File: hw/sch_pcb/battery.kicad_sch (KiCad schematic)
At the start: 88 parts

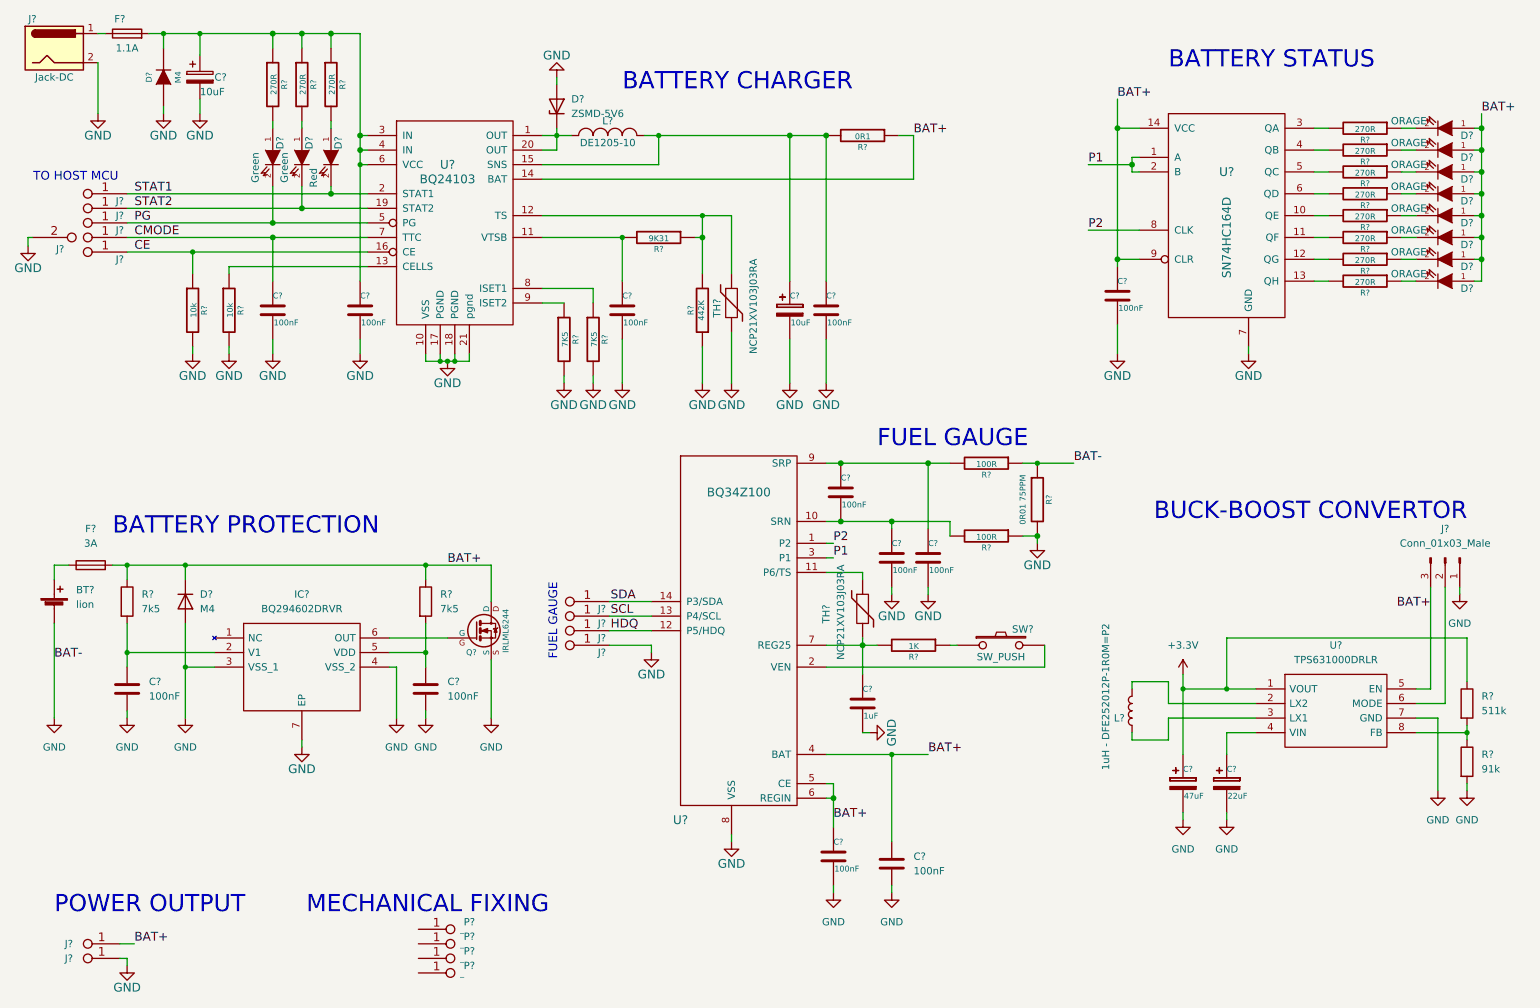
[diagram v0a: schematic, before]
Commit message: schematics update
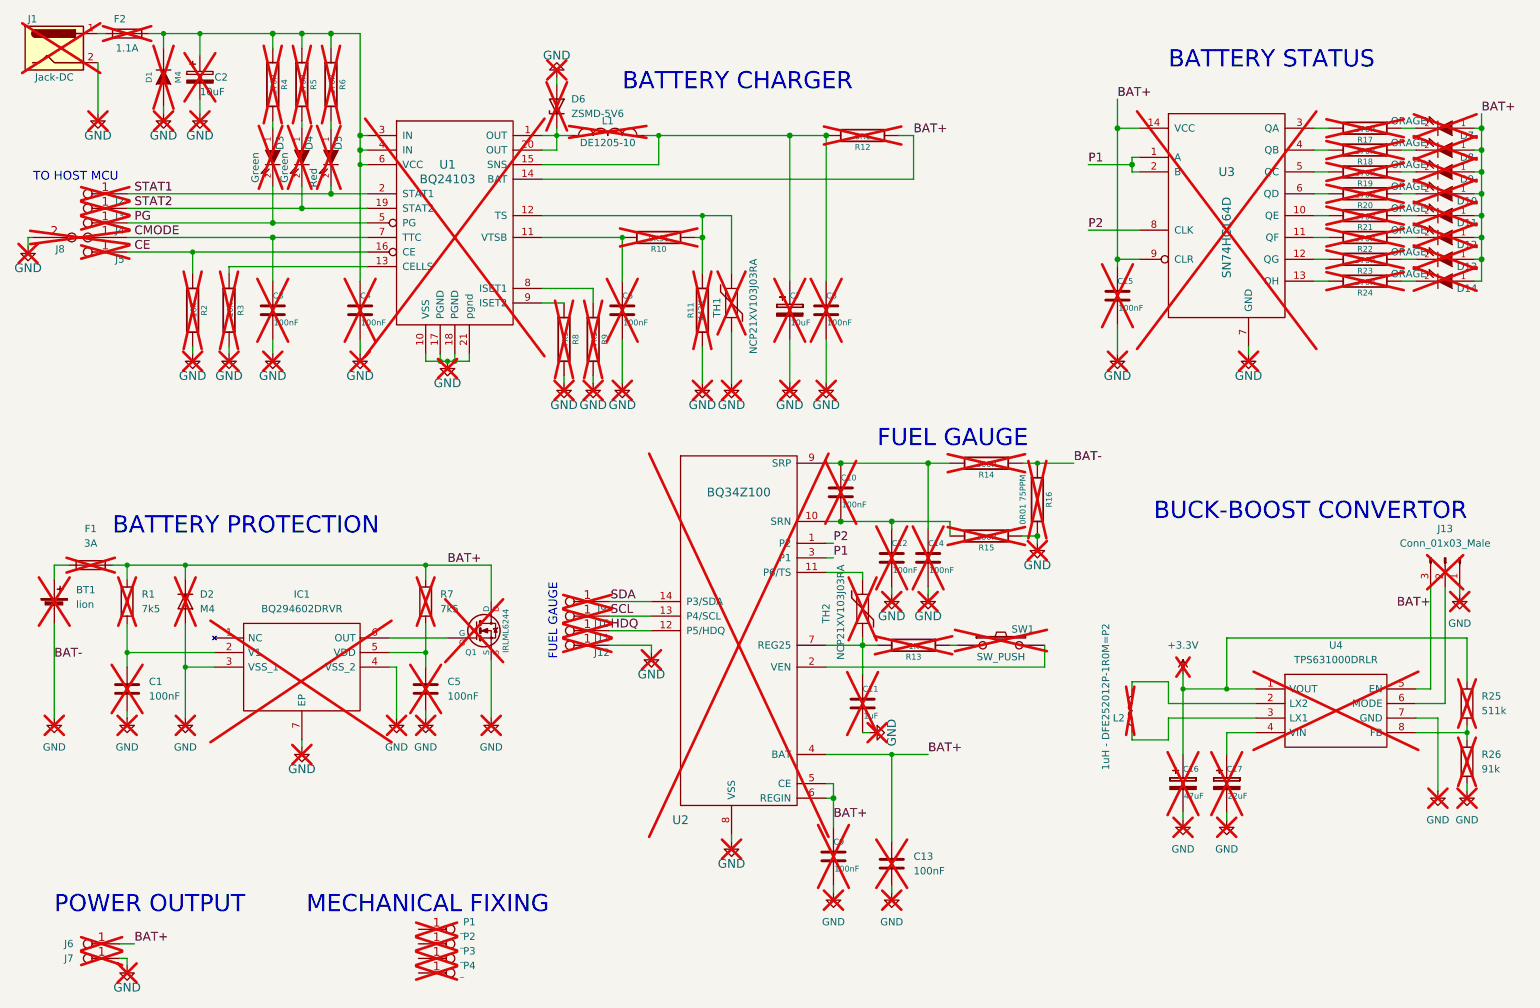
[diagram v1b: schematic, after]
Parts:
- BT1: renamed from BT?; now not fitted; now left out of the parts list
- C1, C10, C11, C12, C13, C14, C15, C16, C17, C2, C3, C4, C5, C6, C7, C8, C9: renamed from C?; now not fitted; now left out of the parts list
- D1, D10, D11, D12, D13, D14, D2, D3, D4, D5, D6, D7, D8, D9: renamed from D?; now not fitted; now left out of the parts list
- F1, F2: renamed from F?; now not fitted; now left out of the parts list
- IC1: renamed from IC?; now not fitted; now left out of the parts list
- J1, J10, J11, J12, J13, J2, J3, J4, J5, J6, J7, J8, J9: renamed from J?; now not fitted; now left out of the parts list
- L1, L2: renamed from L?; now not fitted; now left out of the parts list
- P1, P2, P3, P4: renamed from P?; now not fitted; now left out of the parts list
- Q1: renamed from Q?; now not fitted; now left out of the parts list
- R1, R10, R11, R12, R13, R14, R15, R16, R17, R18, R19, R2, R20, R21, R22, R23, R24, R25, R26, R3, R4, R5, R6, R7, R8, R9: renamed from R?; now not fitted; now left out of the parts list
- SW1: renamed from SW?; now not fitted; now left out of the parts list
- TH1, TH2: renamed from TH?; now not fitted; now left out of the parts list
- U1, U2, U3, U4: renamed from U?; now not fitted; now left out of the parts list
